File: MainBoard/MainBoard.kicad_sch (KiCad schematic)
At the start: 30 parts, among them U1 TL074CN, U2 TL074CN, U3 TL074CN

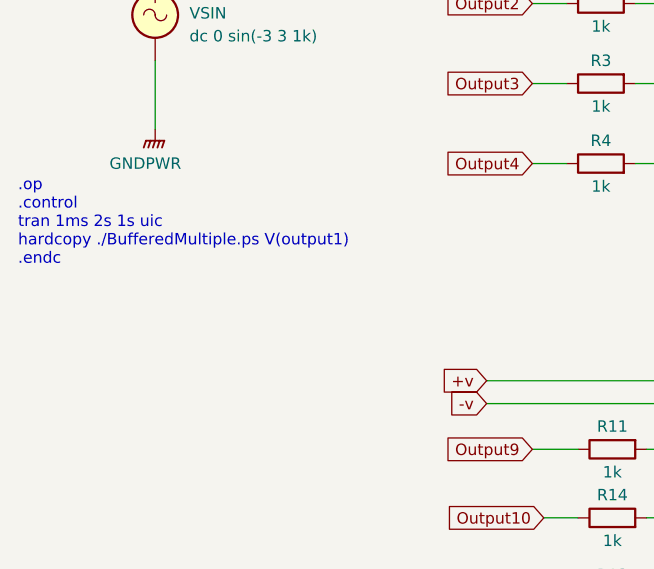
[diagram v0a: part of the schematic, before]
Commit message: updates simulation parameters
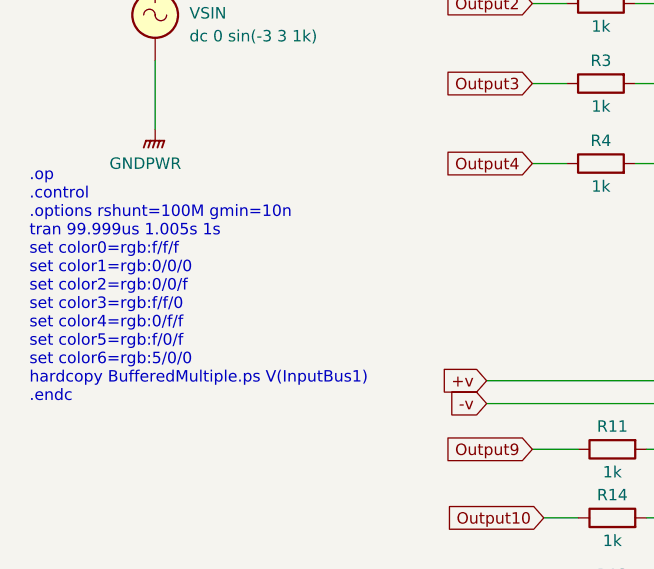
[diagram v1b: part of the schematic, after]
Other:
- note added: ".op .control .options rshunt=100M gmin=10n tran 99.999us 1.005s 1s set color0=rgb:f/f/f set color1=rgb:0/0/0 set color2=rgb:0/0/f set color3=rgb:f/f/0 set color4=rgb:0/f/f set color5=rgb:f/0/f set color6=rgb:5/0/0 hardcopy BufferedMultiple.ps V(InputBus1) .endc"
- note removed: ".op .control tran 1ms 2s 1s uic hardcopy ./BufferedMultiple.ps V(output1) .endc"
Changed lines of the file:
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@@
     (stroke (width 0) (type default) (color 0 0 0 0))
   )
-  (text ".op\n.control\ntran 1ms 2s 1s uic\nhardcopy ./BufferedMultiple.ps V(output1)\n.endc"
-    (at 15.24 74.93 0)
+  (text ".op\n.control\n.options rshunt=100M gmin=10n\ntran 99.999us 1.005s 1s\nset color0=rgb:f/f/f\nset color1=rgb:0/0/0\nset color2=rgb:0/0/f\nset color3=rgb:f/f/0\nset color4=rgb:0/f/f\nset color5=rgb:f/0/f\nset color6=rgb:5/0/0\nhardcopy BufferedMultiple.ps V(InputBus1)\n.endc\n"
+    (at 16.51 90.17 0)
     (effects (font (size 1.27 1.27)) (justify left bottom))
   )

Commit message: added local models
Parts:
- D1, D2: Spice_Lib_File /usr/share/kicad/models/1N5818.mod -> ../models/1N5818.mod
- U1, U2, U3: Spice_Lib_File /usr/share/kicad/models/TL074.mod -> ../models/TL074.mod
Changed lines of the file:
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@@
       (effects (font (size 1.27 1.27)) hide)
     )
-    (property "Spice_Lib_File" "/usr/share/kicad/models/1N5818.mod" (id 7) (at 114.3 152.4 0)
+    (property "Spice_Lib_File" "../models/1N5818.mod" (id 7) (at 114.3 152.4 0)
       (effects (font (size 1.27 1.27)) hide)
     )
@@
       (effects (font (size 1.27 1.27)) hide)
     )
-    (property "Spice_Lib_File" "/usr/share/kicad/models/TL074.mod" (id 7) (at 109.22 43.18 0)
+    (property "Spice_Lib_File" "../models/TL074.mod" (id 7) (at 109.22 43.18 0)
       (effects (font (size 1.27 1.27)) hide)
     )
@@
       (effects (font (size 1.27 1.27)) hide)
     )
-    (property "Spice_Lib_File" "/usr/share/kicad/models/TL074.mod" (id 7) (at 190.5 43.18 0)
+    (property "Spice_Lib_File" "../models/TL074.mod" (id 7) (at 190.5 43.18 0)
       (effects (font (size 1.27 1.27)) hide)
     )
@@
       (effects (font (size 1.27 1.27)) hide)
     )
-    (property "Spice_Lib_File" "/usr/share/kicad/models/TL074.mod" (id 7) (at 109.22 102.87 0)
+    (property "Spice_Lib_File" "../models/TL074.mod" (id 7) (at 109.22 102.87 0)
       (effects (font (size 1.27 1.27)) hide)
     )
@@
       (effects (font (size 1.27 1.27)) hide)
     )
-    (property "Spice_Lib_File" "/usr/share/kicad/models/1N5818.mod" (id 7) (at 114.3 171.45 0)
-      (effects (font (size 1.27 1.27)) hide)
-    )
+    (property "Spice_Lib_File" "../models/1N5818.mod" (id 7) (at 114.3 171.45 0)
+      (effects (font (size 1.27 1.27)) hide)
+    )

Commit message: offset sin stimulus by -1.5v with a 3v peak to peak
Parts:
- Vin1: Spice_Model dc 0 sin(-3 3 1k) -> dc 0 sin(-1.5v 3v 1k)
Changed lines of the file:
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@@
       (effects (font (size 1.27 1.27)) (justify left) hide)
     )
-    (property "Spice_Model" "dc 0 sin(-3 3 1k)" (id 6) (at 34.29 49.3401 0)
+    (property "Spice_Model" "dc 0 sin(-1.5v 3v 1k)" (id 6) (at 34.29 49.3401 0)
       (effects (font (size 1.27 1.27)) (justify left))
     )

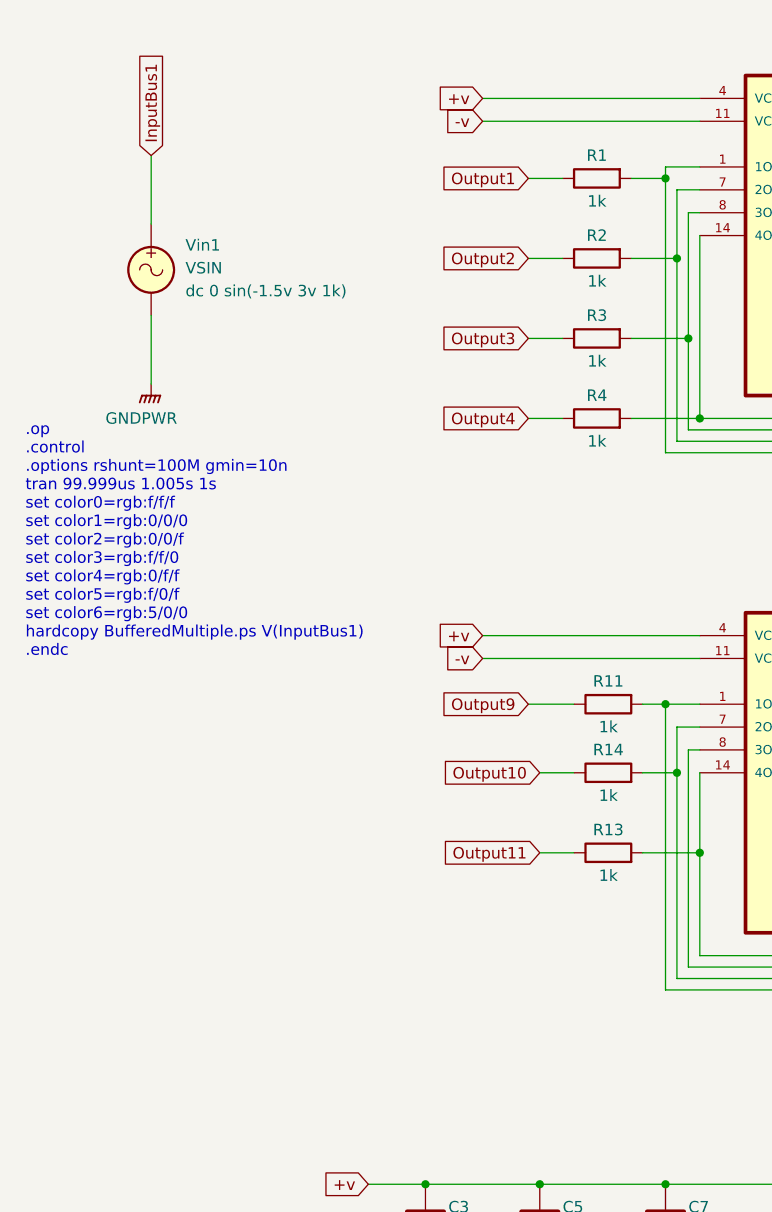
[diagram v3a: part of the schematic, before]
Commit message: added additional output plots for first mult
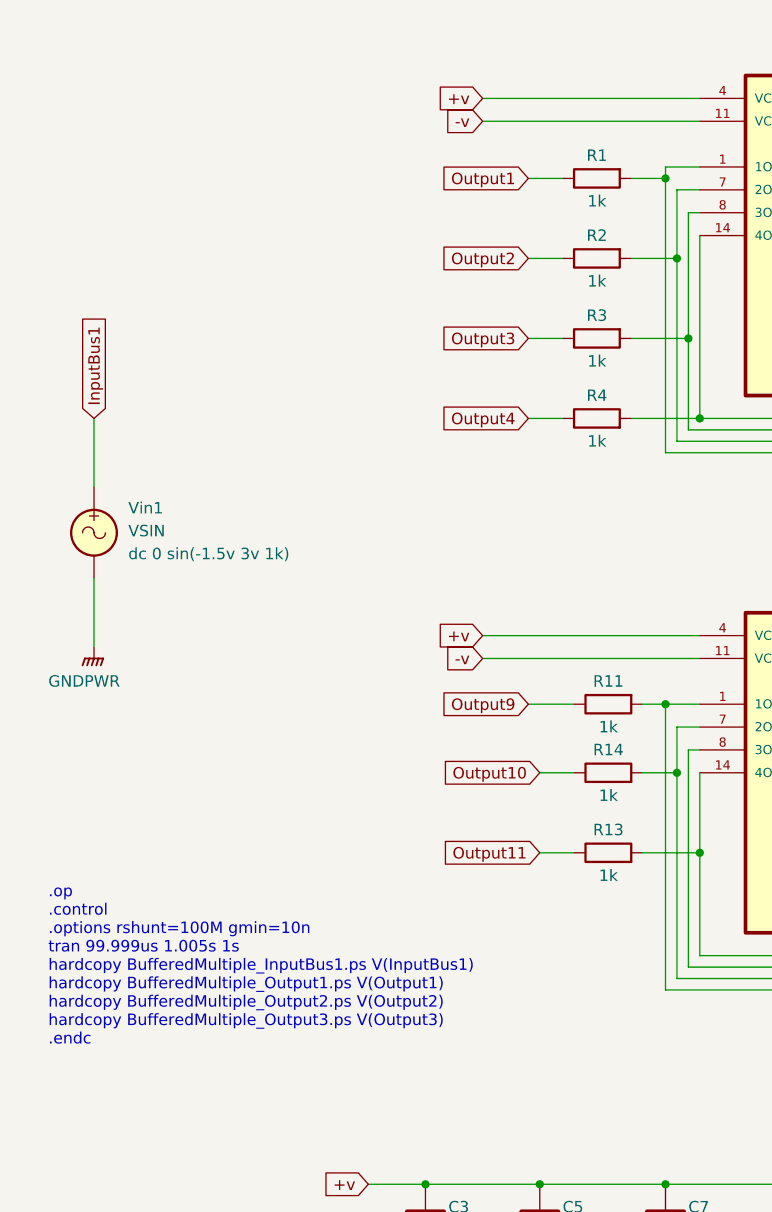
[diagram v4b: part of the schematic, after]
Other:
- note added: ".op .control .options rshunt=100M gmin=10n tran 99.999us 1.005s 1s hardcopy BufferedMultiple_InputBus1.ps V(InputBus1) hardcopy BufferedMultiple_Output1.ps V(Output1) hardcopy BufferedMultiple_Output2.ps V(Output2) hardcopy BufferedMultiple_Output3.ps V(Output3) .endc"
- note removed: ".op .control .options rshunt=100M gmin=10n tran 99.999us 1.005s 1s set color0=rgb:f/f/f set color1=rgb:0/0/0 set color2=rgb:0/0/f set color3=rgb:f/f/0 set color4=rgb:0/f/f set color5=rgb:f/0/f set color6=rgb:5/0/0 hardcopy BufferedMultiple.ps V(InputBus1) .endc"
- moved on the sheet: Vin1
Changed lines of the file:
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@@
     (stroke (width 0) (type default) (color 0 0 0 0))
   )
-  (wire (pts (xy 30.48 52.07) (xy 30.48 59.69))
+  (wire (pts (xy 24.13 81.28) (xy 24.13 88.9))
     (stroke (width 0) (type default) (color 0 0 0 0))
   )
@@
     (stroke (width 0) (type default) (color 0 0 0 0))
   )
-  (wire (pts (xy 30.48 34.29) (xy 30.48 41.91))
+  (wire (pts (xy 24.13 63.5) (xy 24.13 71.12))
     (stroke (width 0) (type default) (color 0 0 0 0))
   )
@@
     (stroke (width 0) (type default) (color 0 0 0 0))
   )
-  (text ".op\n.control\n.options rshunt=100M gmin=10n\ntran 99.999us 1.005s 1s\nset color0=rgb:f/f/f\nset color1=rgb:0/0/0\nset color2=rgb:0/0/f\nset color3=rgb:f/f/0\nset color4=rgb:0/f/f\nset color5=rgb:f/0/f\nset color6=rgb:5/0/0\nhardcopy BufferedMultiple.ps V(InputBus1)\n.endc\n"
-    (at 16.51 90.17 0)
+  (text ".op\n.control\n.options rshunt=100M gmin=10n\ntran 99.999us 1.005s 1s\nhardcopy BufferedMultiple_InputBus1.ps V(InputBus1)\nhardcopy BufferedMultiple_Output1.ps V(Output1)\nhardcopy BufferedMultiple_Output2.ps V(Output2)\nhardcopy BufferedMultiple_Output3.ps V(Output3)\n.endc\n"
+    (at 19.05 133.35 0)
     (effects (font (size 1.27 1.27)) (justify left bottom))
   )
@@
     )
   )
-  (global_label "InputBus1" (shape input) (at 30.48 34.29 90) (fields_autoplaced)
+  (global_label "InputBus1" (shape input) (at 24.13 63.5 90) (fields_autoplaced)
     (effects (font (size 1.27 1.27)) (justify left))
-    (property "Intersheet References" "${INTERSHEET_REFS}" (id 0) (at 30.4006 22.4426 90)
+    (property "Intersheet References" "${INTERSHEET_REFS}" (id 0) (at 24.0506 51.6526 90)
       (effects (font (size 1.27 1.27)) (justify right) hide)
     )
@@
     (pin "2")
   )
-  (symbol (lib_id "power:GNDPWR") (at 30.48 59.69 0) (unit 1)
+  (symbol (lib_id "power:GNDPWR") (at 24.13 88.9 0) (unit 1)
     (in_bom no) (on_board no)
-    (property "Reference" "#PWR0109" (id 0) (at 30.48 64.77 0)
-      (effects (font (size 1.27 1.27)) hide)
-    )
-    (property "Value" "GNDPWR" (id 1) (at 25.4 63.5 0)
-      (effects (font (size 1.27 1.27)) (justify left))
-    )
-    (property "Footprint" "" (id 2) (at 30.48 60.96 0)
-      (effects (font (size 1.27 1.27)) hide)
-    )
-    (property "Datasheet" "" (id 3) (at 30.48 60.96 0)
+    (property "Reference" "#PWR0109" (id 0) (at 24.13 93.98 0)
+      (effects (font (size 1.27 1.27)) hide)
+    )
+    (property "Value" "GNDPWR" (id 1) (at 19.05 92.71 0)
+      (effects (font (size 1.27 1.27)) (justify left))
+    )
+    (property "Footprint" "" (id 2) (at 24.13 90.17 0)
+      (effects (font (size 1.27 1.27)) hide)
+    )
+    (property "Datasheet" "" (id 3) (at 24.13 90.17 0)
       (effects (font (size 1.27 1.27)) hide)
     )
@@
     (pin "2")
   )
-  (symbol (lib_id "Simulation_SPICE:VSIN") (at 30.48 46.99 0) (unit 1)
+  (symbol (lib_id "Simulation_SPICE:VSIN") (at 24.13 76.2 0) (unit 1)
     (in_bom no) (on_board no) (fields_autoplaced)
-    (property "Reference" "Vin1" (id 0) (at 34.29 44.2601 0)
-      (effects (font (size 1.27 1.27)) (justify left))
-    )
-    (property "Value" "VSIN" (id 1) (at 34.29 46.8001 0)
-      (effects (font (size 1.27 1.27)) (justify left))
-    )
-    (property "Footprint" "" (id 2) (at 30.48 46.99 0)
-      (effects (font (size 1.27 1.27)) hide)
-    )
-    (property "Datasheet" "~" (id 3) (at 30.48 46.99 0)
-      (effects (font (size 1.27 1.27)) hide)
-    )
-    (property "Spice_Netlist_Enabled" "Y" (id 4) (at 30.48 46.99 0)
+    (property "Reference" "Vin1" (id 0) (at 27.94 73.4701 0)
+      (effects (font (size 1.27 1.27)) (justify left))
+    )
+    (property "Value" "VSIN" (id 1) (at 27.94 76.0101 0)
+      (effects (font (size 1.27 1.27)) (justify left))
+    )
+    (property "Footprint" "" (id 2) (at 24.13 76.2 0)
+      (effects (font (size 1.27 1.27)) hide)
+    )
+    (property "Datasheet" "~" (id 3) (at 24.13 76.2 0)
+      (effects (font (size 1.27 1.27)) hide)
+    )
+    (property "Spice_Netlist_Enabled" "Y" (id 4) (at 24.13 76.2 0)
       (effects (font (size 1.27 1.27)) (justify left) hide)
     )
-    (property "Spice_Primitive" "V" (id 5) (at 30.48 46.99 0)
+    (property "Spice_Primitive" "V" (id 5) (at 24.13 76.2 0)
       (effects (font (size 1.27 1.27)) (justify left) hide)
     )
-    (property "Spice_Model" "dc 0 sin(-1.5v 3v 1k)" (id 6) (at 34.29 49.3401 0)
-      (effects (font (size 1.27 1.27)) (justify left))
-    )
+    (property "Spice_Model" "dc 0 sin(-1.5v 3v 1k)" (id 6) (at 27.94 78.5501 0)
+      (effects (font (size 1.27 1.27)) (justify left))
+    )

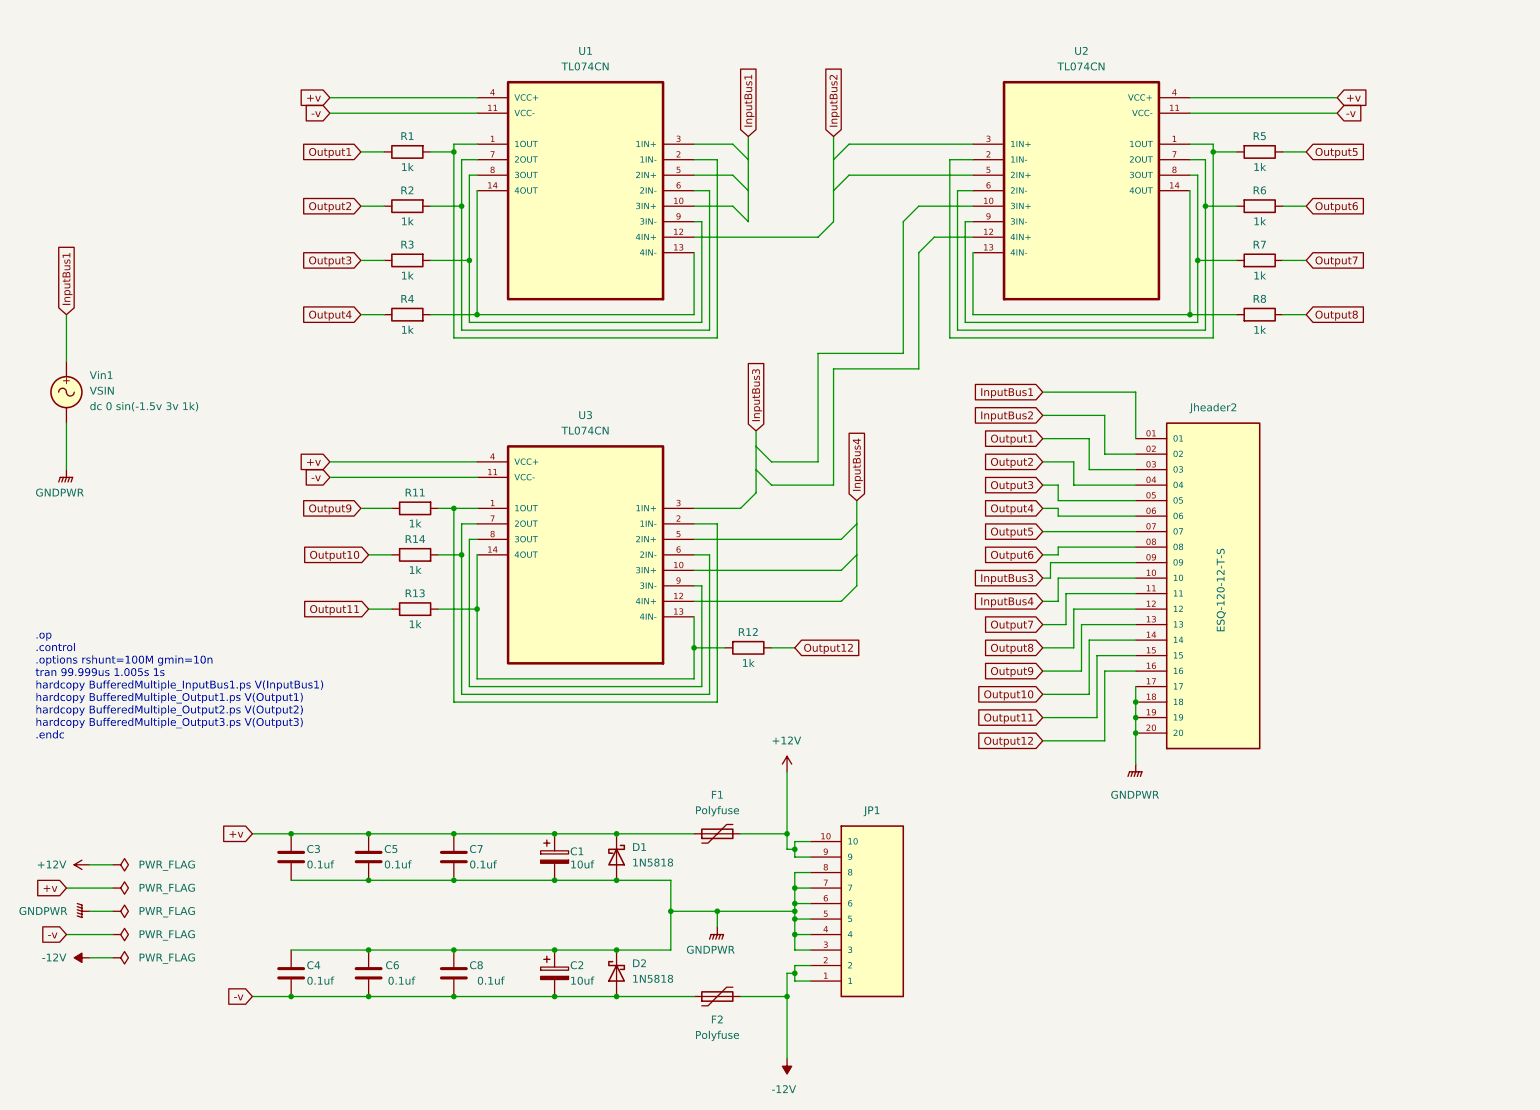
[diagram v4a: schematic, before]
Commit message: added 1M shunt on 1st input so op-amp inputs aren't floating when no signal is plugged in.  Added 100k input resistors to each input. Updated ground to standard GND symbol. Added plot diretory to store ngspice hardcopy plots.
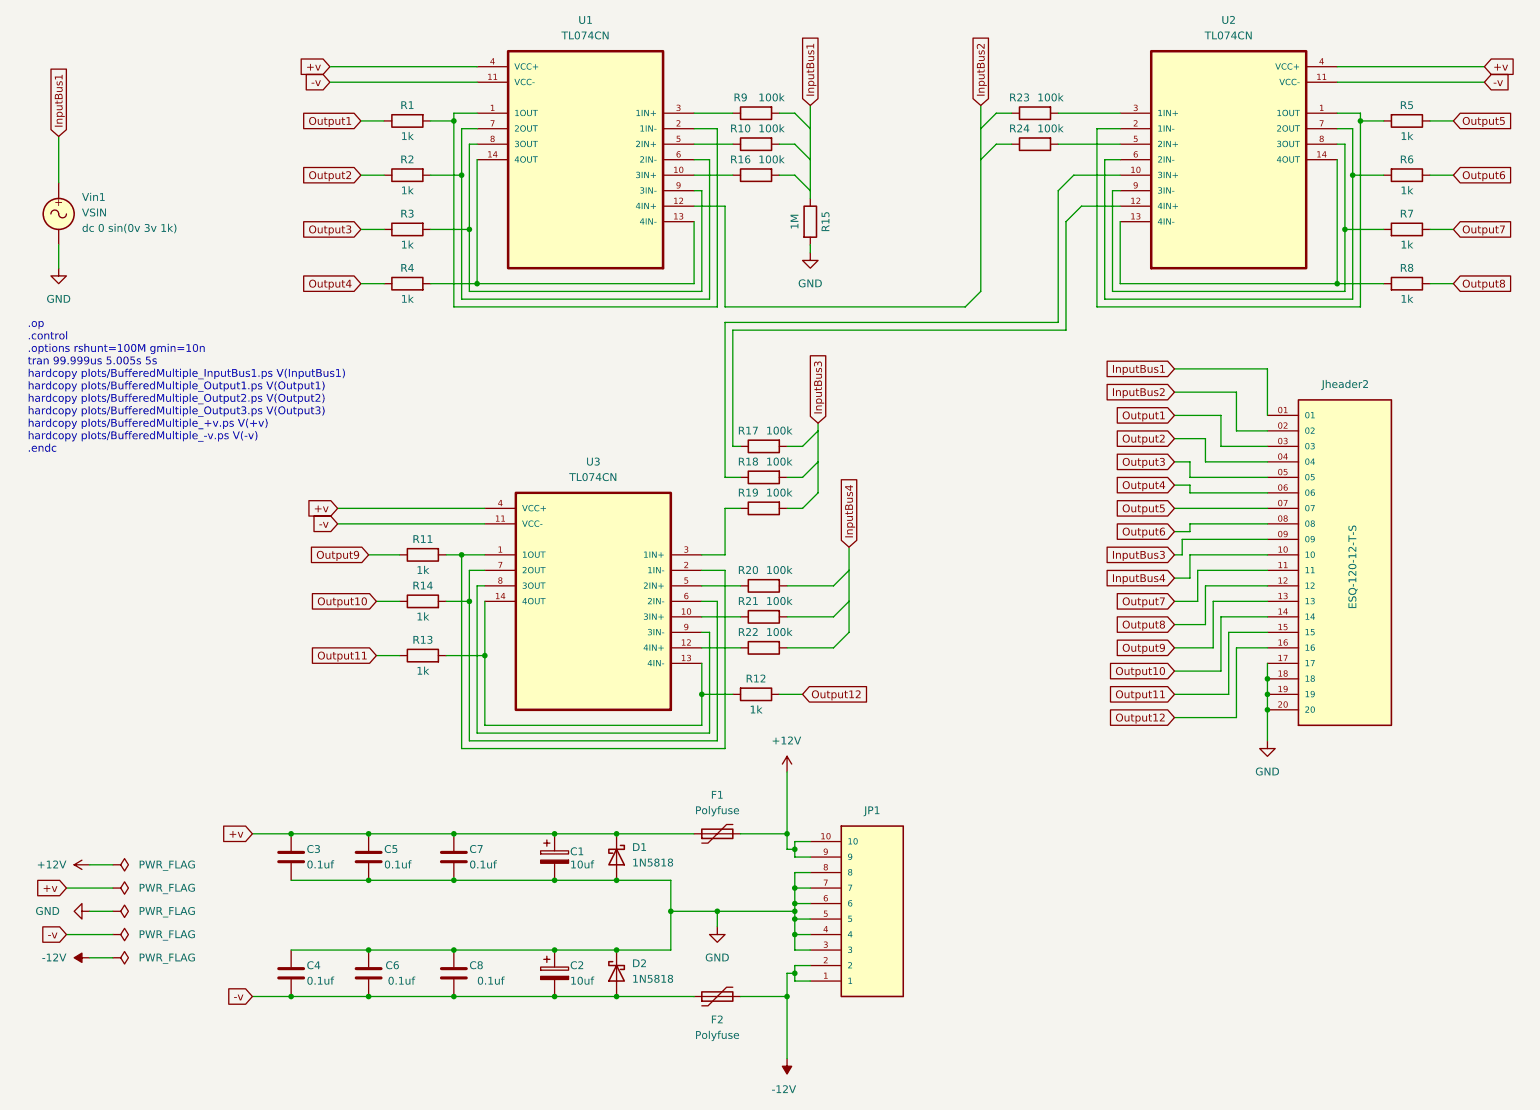
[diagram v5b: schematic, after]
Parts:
- added R10, R16, R17, R18, R19, R20, R21, R22, R23, R24, R9: 100k, Resistor_THT:R_Axial_DIN0204_L3.6mm_D1.6mm_P2.54mm_Vertical, symbol Device:R
- added R15: 1M, Resistor_THT:R_Axial_DIN0204_L3.6mm_D1.6mm_P2.54mm_Vertical, symbol Device:R
- Vin1: Spice_Model dc 0 sin(-1.5v 3v 1k) -> dc 0 sin(0v 3v 1k)
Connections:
- net InputBus1: now also R15.1
- net at U1.10 (3IN+): now also R16.1
- net at U1.3 (1IN+): now also R9.1
- net at U1.5 (2IN+): now also R10.1
- net at U2.3 (1IN+): now also R23.2
- net at U2.5 (2IN+): now also R24.2
- net at U3.10 (3IN+): now also R21.1
- net at U3.12 (4IN+): now also R22.1
- net at U3.3 (1IN+): now also R19.1
- net at U3.5 (2IN+): now also R20.1
- net GNDPWR renamed GND
- net GND: now also R15.2
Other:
- note added: ".op .control .options rshunt=100M gmin=10n tran 99.999us 5.005s 5s hardcopy plots/BufferedMultiple_InputBus1.ps V(InputBus1) hardcopy plots/BufferedMultiple_Output1.ps V(Output1) hardcopy plots/BufferedMultiple_Output2.ps V(Output2) hardcopy plots/BufferedMultiple_Output3.ps V(Output3) hardcopy plots/BufferedMultiple_+v.ps V(+v) hardcopy plots/BufferedMultiple_-v.ps V(-v) .endc"
- note removed: ".op .control .options rshunt=100M gmin=10n tran 99.999us 1.005s 1s hardcopy BufferedMultiple_InputBus1.ps V(InputBus1) hardcopy BufferedMultiple_Output1.ps V(Output1) hardcopy BufferedMultiple_Output2.ps V(Output2) hardcopy BufferedMultiple_Output3.ps V(Output3) .endc"
- moved on the sheet: Jheader2, R1, R11, R12, R13, R14, R2, R3, R4, R5, R6, R7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
